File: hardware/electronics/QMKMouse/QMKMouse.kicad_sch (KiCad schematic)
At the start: 0 parts

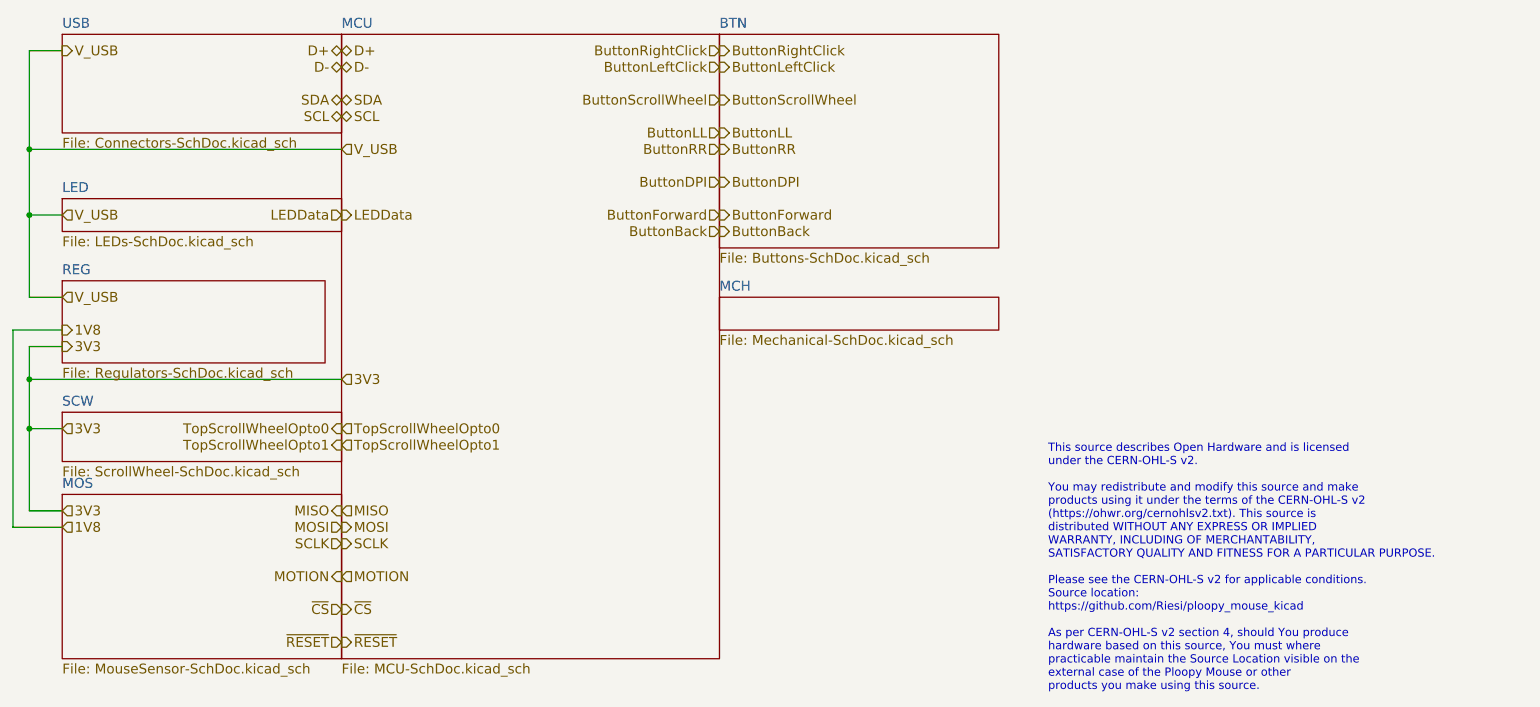
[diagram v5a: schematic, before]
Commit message: fix ERC errors and use hierarchy labels
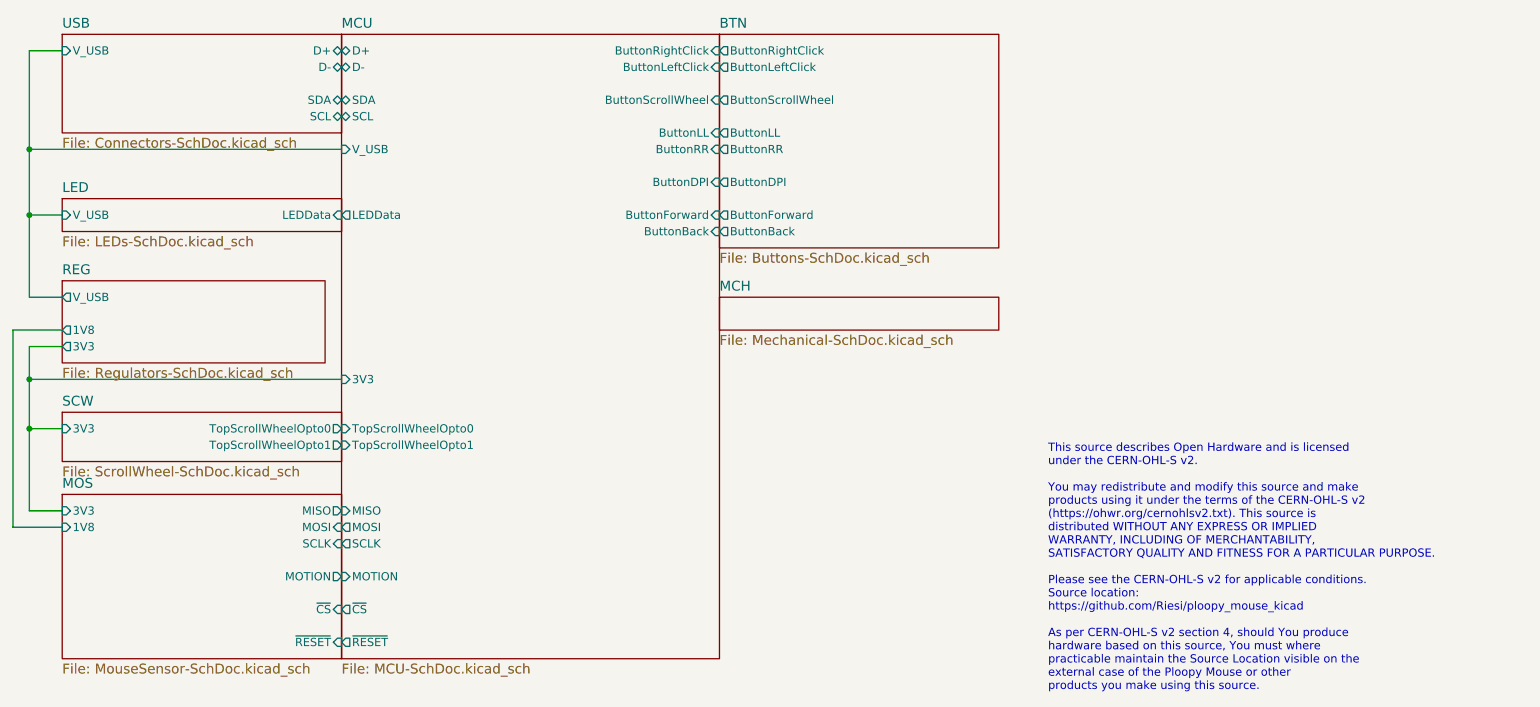
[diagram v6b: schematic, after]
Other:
- sheet BTN ports: added ButtonBack, ButtonDPI, ButtonForward, ButtonLL, ButtonLeftClick, ButtonRR, ButtonRightClick, ButtonScrollWheel; removed none
- sheet LED ports: added LEDData, V_USB; removed none
- sheet MCU ports: added 3V3, ButtonBack, ButtonDPI, ButtonForward, ButtonLL, ButtonLeftClick, ButtonRR, ButtonRightClick, ButtonScrollWheel, D+, D-, LEDData, MISO, MOSI, MOTION, SCL, SCLK, SDA, TopScrollWheelOpto0, TopScrollWheelOpto1, V_USB, ~{CS}, ~{RESET}; removed none
- sheet MOS ports: added 1V8, 3V3, MISO, MOSI, MOTION, SCLK, ~{CS}, ~{RESET}; removed none
- sheet REG ports: added 1V8, 3V3, V_USB; removed none
- sheet SCW ports: added 3V3, TopScrollWheelOpto0, TopScrollWheelOpto1; removed none
- sheet USB ports: added D+, D-, SCL, SDA, V_USB; removed none

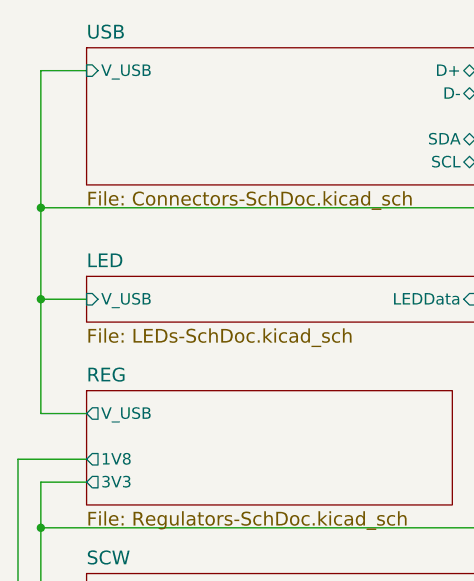
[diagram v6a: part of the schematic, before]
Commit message: Fix all ERC errors and replot the schematic
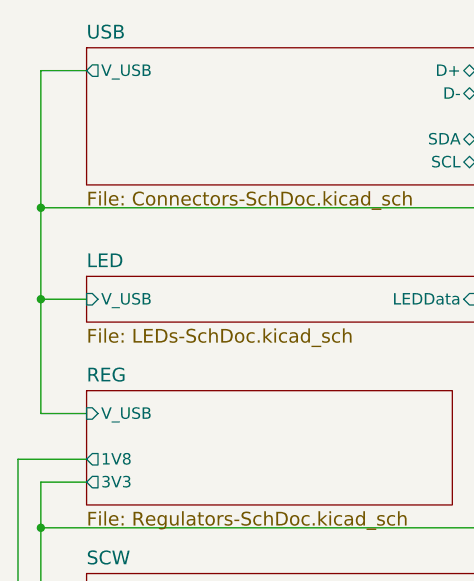
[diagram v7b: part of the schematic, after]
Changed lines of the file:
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@@
+    (stroke (width 0) (type default) (color 0 0 0 0))
+  )
+  (wire (pts (xy 54.61 95.25) (xy 59.69 95.25))
     (stroke (width 0) (type default) (color 0 0 0 0))
   )
@@
   )
   (wire (pts (xy 102.87 72.39) (xy 54.61 72.39))
-    (stroke (width 0) (type default) (color 0 0 0 0))
-  )
-  (wire (pts (xy 59.69 95.25) (xy 54.61 95.25))
     (stroke (width 0) (type default) (color 0 0 0 0))
   )
@@
       (effects (font (size 1.27 1.27)) (justify left))
     )
-    (pin "V_USB" output (at 59.69 95.25 180)
+    (pin "V_USB" input (at 59.69 95.25 180)
       (effects (font (size 1.27 1.27)) (justify left))
     )
@@
       (effects (font (size 1.27 1.27)) (justify right))
     )
-    (pin "V_USB" input (at 59.69 57.15 180)
+    (pin "V_USB" output (at 59.69 57.15 180)
       (effects (font (size 1.27 1.27)) (justify left))
     )
@@
   )
   (symbol_instances
+    (path "/edd86220-f5f9-4f6e-b5ac-222411c977fd/3fcbfa4a-7163-4389-a62b-b401185d53ff"
+      (reference "#FLG0101") (unit 1) (value "PWR_FLAG") (footprint "")
+    )
     (path "/143b26bf-3d77-4275-b4b3-9422596a1eca/00000000-0000-0000-0000-000063c6e54a"
       (reference "#GND0101") (unit 1) (value "GND") (footprint "")
